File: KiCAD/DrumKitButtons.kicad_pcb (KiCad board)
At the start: 2 copper layers, 38 parts, among them U1 74HC165, U2 TLC5916, U3 74HC165, U4 TLC5916

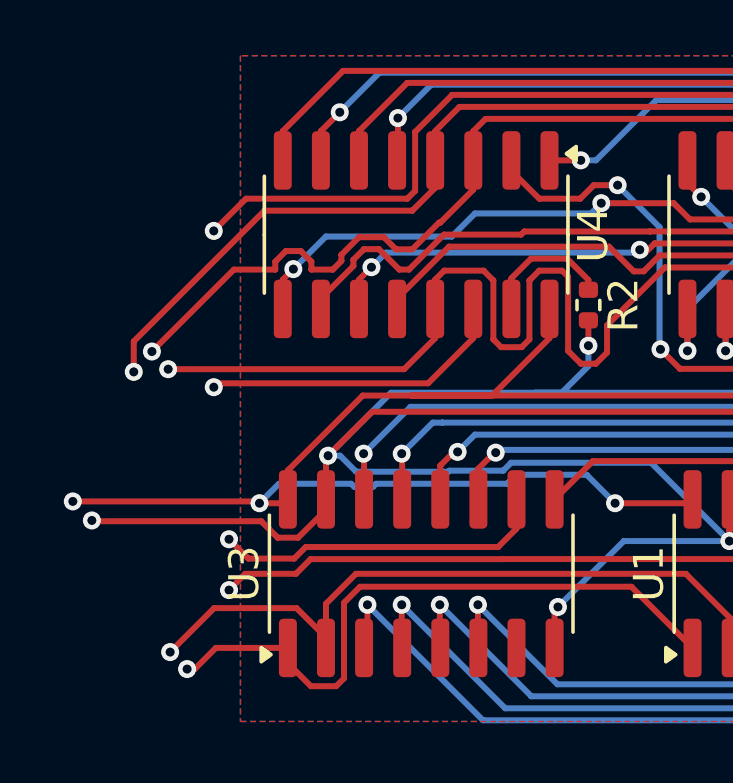
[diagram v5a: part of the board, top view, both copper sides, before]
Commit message: Rework single row to use more of the vertical space between button contacts.
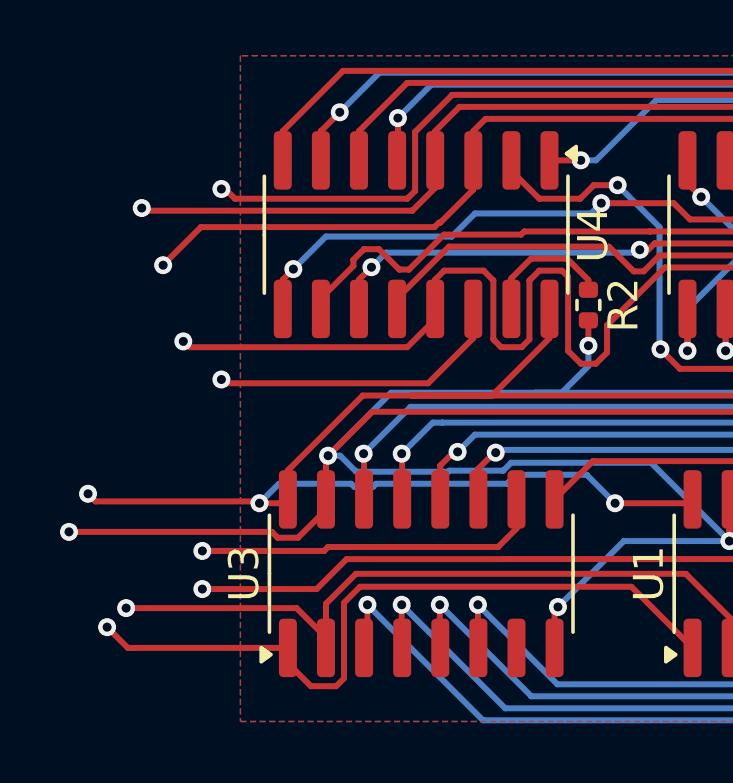
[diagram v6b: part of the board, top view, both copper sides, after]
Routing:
- net LE_{LED}: track 36.2 -> 33.2 mm
- net CLK_{LED}: track 31.1 -> 28.2 mm
- net ~{PL_{SW}}: track 21.2 -> 23.8 mm
- net ~{OE_{LED}}: track 35.0 -> 33.9 mm
- net /DO_{SW}: track 26.2 -> 27.0 mm
- net CLK_{SW}: track 23.2 -> 24.0 mm
- net GND: track 135.9 -> 136.5 mm
- net /DI_{LED}: track 28.3 -> 27.7 mm
- net /DI_{SW}: track 11.2 -> 11.8 mm

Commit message: Add 3 rows again
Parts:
- added H1: MountingHole, MountingHole:MountingHole_3.2mm_M3, F.Cu at (84.4, 55.1)
- added H2: MountingHole, MountingHole:MountingHole_3.2mm_M3, F.Cu at (349.2, 45.0)
- added H3: MountingHole, MountingHole:MountingHole_3.2mm_M3, F.Cu at (367.0, 56.7)
- added H4: MountingHole, MountingHole:MountingHole_3.2mm_M3, F.Cu at (349.2, 69.7)
- added J1: Output, Connector_PinHeader_2.54mm:PinHeader_1x09_P2.54mm_Vertical, F.Cu at (84.4, 43.1)
- added J2: Input, Connector_PinHeader_2.54mm:PinHeader_1x09_P2.54mm_Vertical, F.Cu at (84.4, 68.5)
- added R19: 1.6kΩ, Resistor_SMD:R_0402_1005Metric, F.Cu at (117.0, 55.8)
- added R20: 1.6kΩ, Resistor_SMD:R_0402_1005Metric, F.Cu at (105.5, 53.9)
- added R21: 47Ω, Resistor_SMD:R_0402_1005Metric, F.Cu at (137.7, 61.3)
- added R22: 47Ω, Resistor_SMD:R_0402_1005Metric, F.Cu at (152.5, 61.3)
- added R23: 47Ω, Resistor_SMD:R_0402_1005Metric, F.Cu at (167.9, 61.3)
- added R24: 47Ω, Resistor_SMD:R_0402_1005Metric, F.Cu at (182.6, 61.1)
- added R25: 47Ω, Resistor_SMD:R_0402_1005Metric, F.Cu at (197.6, 61.3)
- added R26: 47Ω, Resistor_SMD:R_0402_1005Metric, F.Cu at (212.7, 61.3)
- added R27: 47Ω, Resistor_SMD:R_0402_1005Metric, F.Cu at (227.7, 61.3)
- added R28: 47Ω, Resistor_SMD:R_0402_1005Metric, F.Cu at (242.7, 61.3)
- added R29: 47Ω, Resistor_SMD:R_0402_1005Metric, F.Cu at (257.7, 61.3)
- added R30: 47Ω, Resistor_SMD:R_0402_1005Metric, F.Cu at (272.7, 61.3)
- added R31: 47Ω, Resistor_SMD:R_0402_1005Metric, F.Cu at (287.6, 61.3)
- added R32: 47Ω, Resistor_SMD:R_0402_1005Metric, F.Cu at (302.6, 61.3)
- added R33: 47Ω, Resistor_SMD:R_0402_1005Metric, F.Cu at (317.7, 61.3)
- added R34: 47Ω, Resistor_SMD:R_0402_1005Metric, F.Cu at (332.6, 61.3)
- added R35: 47Ω, Resistor_SMD:R_0402_1005Metric, F.Cu at (347.7, 61.3)
- added R36: 47Ω, Resistor_SMD:R_0402_1005Metric, F.Cu at (356.0, 64.8)
- added R37: 1.6kΩ, Resistor_SMD:R_0402_1005Metric, F.Cu at (117.0, 81.2)
- added R38: 1.6kΩ, Resistor_SMD:R_0402_1005Metric, F.Cu at (105.5, 79.3)
- added R39: 47Ω, Resistor_SMD:R_0402_1005Metric, F.Cu at (137.7, 86.7)
- added R40: 47Ω, Resistor_SMD:R_0402_1005Metric, F.Cu at (152.5, 86.7)
- added R41: 47Ω, Resistor_SMD:R_0402_1005Metric, F.Cu at (167.9, 86.7)
- added R42: 47Ω, Resistor_SMD:R_0402_1005Metric, F.Cu at (182.6, 86.5)
- added R43: 47Ω, Resistor_SMD:R_0402_1005Metric, F.Cu at (197.6, 86.7)
- added R44: 47Ω, Resistor_SMD:R_0402_1005Metric, F.Cu at (212.7, 86.7)
- added R45: 47Ω, Resistor_SMD:R_0402_1005Metric, F.Cu at (227.7, 86.7)
- added R46: 47Ω, Resistor_SMD:R_0402_1005Metric, F.Cu at (242.7, 86.7)
- added R47: 47Ω, Resistor_SMD:R_0402_1005Metric, F.Cu at (257.7, 86.7)
- added R48: 47Ω, Resistor_SMD:R_0402_1005Metric, F.Cu at (272.7, 86.7)
- added R49: 47Ω, Resistor_SMD:R_0402_1005Metric, F.Cu at (287.6, 86.7)
- added R50: 47Ω, Resistor_SMD:R_0402_1005Metric, F.Cu at (302.6, 86.7)
- added R51: 47Ω, Resistor_SMD:R_0402_1005Metric, F.Cu at (317.7, 86.7)
- added R52: 47Ω, Resistor_SMD:R_0402_1005Metric, F.Cu at (332.6, 86.7)
- added R53: 47Ω, Resistor_SMD:R_0402_1005Metric, F.Cu at (347.7, 86.7)
- added R54: 47Ω, Resistor_SMD:R_0402_1005Metric, F.Cu at (356.0, 90.2)
- added SW17: ~, Local:PB86, B.Cu at (130.8, 55.6)
- added SW18: ~, Local:PB86, B.Cu at (145.8, 55.6)
- added SW19: ~, Local:PB86, B.Cu at (160.8, 55.6)
- added SW20: ~, Local:PB86, B.Cu at (175.8, 55.6)
- added SW21: ~, Local:PB86, B.Cu at (190.8, 55.6)
- added SW22: ~, Local:PB86, B.Cu at (205.8, 55.6)
- added SW23: ~, Local:PB86, B.Cu at (220.8, 55.6)
- added SW24: ~, Local:PB86, B.Cu at (235.8, 55.6)
- added SW25: ~, Local:PB86, B.Cu at (250.8, 55.6)
- added SW26: ~, Local:PB86, B.Cu at (265.8, 55.6)
- added SW27: ~, Local:PB86, B.Cu at (280.8, 55.6)
- added SW28: ~, Local:PB86, B.Cu at (295.8, 55.6)
- added SW29: ~, Local:PB86, B.Cu at (310.8, 55.6)
- added SW30: ~, Local:PB86, B.Cu at (325.8, 55.6)
- added SW31: ~, Local:PB86, B.Cu at (340.8, 55.6)
- added SW32: ~, Local:PB86, B.Cu at (355.8, 55.6)
- added SW33: ~, Local:PB86, B.Cu at (130.8, 81.0)
- added SW34: ~, Local:PB86, B.Cu at (145.8, 81.0)
- added SW35: ~, Local:PB86, B.Cu at (160.8, 81.0)
- added SW36: ~, Local:PB86, B.Cu at (175.8, 81.0)
- added SW37: ~, Local:PB86, B.Cu at (190.8, 81.0)
- added SW38: ~, Local:PB86, B.Cu at (205.8, 81.0)
- added SW39: ~, Local:PB86, B.Cu at (220.8, 81.0)
- added SW40: ~, Local:PB86, B.Cu at (235.8, 81.0)
- added SW41: ~, Local:PB86, B.Cu at (250.8, 81.0)
- added SW42: ~, Local:PB86, B.Cu at (265.8, 81.0)
- added SW43: ~, Local:PB86, B.Cu at (280.8, 81.0)
- added SW44: ~, Local:PB86, B.Cu at (295.8, 81.0)
- added SW45: ~, Local:PB86, B.Cu at (310.8, 81.0)
- added SW46: ~, Local:PB86, B.Cu at (325.8, 81.0)
- added SW47: ~, Local:PB86, B.Cu at (340.8, 81.0)
- added SW48: ~, Local:PB86, B.Cu at (355.8, 81.0)
- added U10: 74HC165, Package_SO:SOIC-16_3.9x9.9mm_P1.27mm, F.Cu at (99.9, 88.3)
- added U11: TLC5916, Package_SO:SOIC-16_3.9x9.9mm_P1.27mm, F.Cu at (113.3, 77.0)
- added U12: TLC5916, Package_SO:SOIC-16_3.9x9.9mm_P1.27mm, F.Cu at (99.8, 77.0)
- added U5: 74HC165, Package_SO:SOIC-16_3.9x9.9mm_P1.27mm, F.Cu at (113.4, 62.9)
- added U6: 74HC165, Package_SO:SOIC-16_3.9x9.9mm_P1.27mm, F.Cu at (99.9, 62.9)
- added U7: TLC5916, Package_SO:SOIC-16_3.9x9.9mm_P1.27mm, F.Cu at (113.3, 51.6)
- added U8: TLC5916, Package_SO:SOIC-16_3.9x9.9mm_P1.27mm, F.Cu at (99.8, 51.6)
- added U9: 74HC165, Package_SO:SOIC-16_3.9x9.9mm_P1.27mm, F.Cu at (113.4, 88.3)
- moved R1 50.8 mm to (117.0, 30.4)
- moved R17 50.8 mm to (347.7, 35.9)
- moved R3 50.8 mm to (137.7, 35.9)
- moved R4 50.8 mm to (152.5, 35.9)
- moved R6 50.8 mm to (182.6, 35.7)
- moved U1 50.8 mm to (113.4, 37.5)
- moved U3 50.8 mm to (99.9, 37.5)
- moved R10 50.8 mm to (242.7, 35.9)
- moved R11 50.8 mm to (257.7, 35.9)
- moved R12 50.8 mm to (272.7, 35.9)
- moved R13 50.8 mm to (287.6, 35.9)
- moved R14 50.8 mm to (302.6, 35.9)
- moved R15 50.8 mm to (317.7, 35.9)
- moved R16 50.8 mm to (332.6, 35.9)
- moved R18 50.8 mm to (356.0, 39.4)
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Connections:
- U3 pad 10: /DI_{SW} -> /Button Bank 1/DI_{SW}
- U4 pad 14: /DO_{LED} -> /Button Bank 1/DO_{LED}
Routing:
- net VCC: track 399.8 -> 1330.4 mm, vias 3 -> 9
- net GND: track 136.5 -> 479.8 mm, vias 9 -> 27
- net /Button Bank 5/SW_{7}: track 0.00 -> 267.3 mm, vias 0 -> 2
- net /Button Bank 3/SW_{7}: track 0.00 -> 267.3 mm, vias 0 -> 2
- net /Button Bank 5/LED_{7}: track 0.00 -> 262.7 mm, vias 0 -> 1
- net /Button Bank 3/LED_{7}: track 0.00 -> 262.7 mm, vias 0 -> 1
- net /Button Bank 5/SW_{6}: track 0.00 -> 254.0 mm, vias 0 -> 1
- net /Button Bank 3/SW_{6}: track 0.00 -> 254.0 mm, vias 0 -> 1
- net /Button Bank 3/LED_{6}: track 0.00 -> 249.0 mm, vias 0 -> 3
- net /Button Bank 5/LED_{6}: track 0.00 -> 249.0 mm, vias 0 -> 3
- net /Button Bank 5/SW_{5}: track 0.00 -> 237.3 mm, vias 0 -> 1
- net /Button Bank 3/SW_{5}: track 0.00 -> 237.3 mm, vias 0 -> 1
- net /Button Bank 5/LED_{5}: track 0.00 -> 235.2 mm, vias 0 -> 1
- net /Button Bank 3/LED_{5}: track 0.00 -> 235.2 mm, vias 0 -> 1
- net /Button Bank 5/LED_{4}: track 0.00 -> 221.9 mm, vias 0 -> 3
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
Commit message: edge cuts and mounting holes
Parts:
- removed the H3 at (367.0, 56.7)
- added H3: MountingHole, MountingHole:MountingHole_3.2mm_M3, F.Cu at (78.0, 90.7)
- added H3: MountingHole, MountingHole:MountingHole_3.2mm_M3, F.Cu at (157.0, 68.5)
- added H3: MountingHole, MountingHole:MountingHole_3.2mm_M3, F.Cu at (247.0, 43.1)
- added H3: MountingHole, MountingHole:MountingHole_3.2mm_M3, F.Cu at (157.0, 43.1)
- added H3: MountingHole, MountingHole:MountingHole_3.2mm_M3, F.Cu at (365.7, 58.3)
- added H3: MountingHole, MountingHole:MountingHole_3.2mm_M3, F.Cu at (247.0, 68.5)
- moved H1 31.1 mm to (78.0, 24.7)
- moved H4 26.7 mm to (365.7, 90.7)
- moved H2 26.2 mm to (365.7, 24.7)
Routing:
- net /Button Bank 1/SW_{7}: track 267.3 -> 271.6 mm
- net /Button Bank 1/SW_{6}: track 254.0 -> 256.6 mm
- net /Button Bank 1/SW_{5}: track 237.3 -> 239.9 mm
- net /Button Bank 1/SW_{4}: track 220.8 -> 223.4 mm
- net /Button Bank 1/SW_{3}: track 206.4 -> 209.0 mm
- net /Button Bank 1/SW_{2}: track 192.8 -> 195.4 mm
- net /Button Bank 1/SW_{1}: track 179.3 -> 181.9 mm
- net /Button Bank 3/SW_{6}: track 254.0 -> 256.5 mm
- net /Button Bank 3/SW_{5}: track 237.3 -> 239.8 mm
- net /Button Bank 3/SW_{7}: track 267.3 -> 269.8 mm
- net /Button Bank 3/SW_{4}: track 220.8 -> 223.2 mm
- net /Button Bank 3/SW_{3}: track 206.4 -> 208.8 mm
- net /Button Bank 3/SW_{2}: track 192.8 -> 195.2 mm
- net /Button Bank 3/SW_{1}: track 179.3 -> 181.7 mm
- net VCC: track 1330.4 -> 1328.3 mm
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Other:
- board outline added: 297.2 x 76.2 mm
